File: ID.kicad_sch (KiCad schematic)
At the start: 25 parts

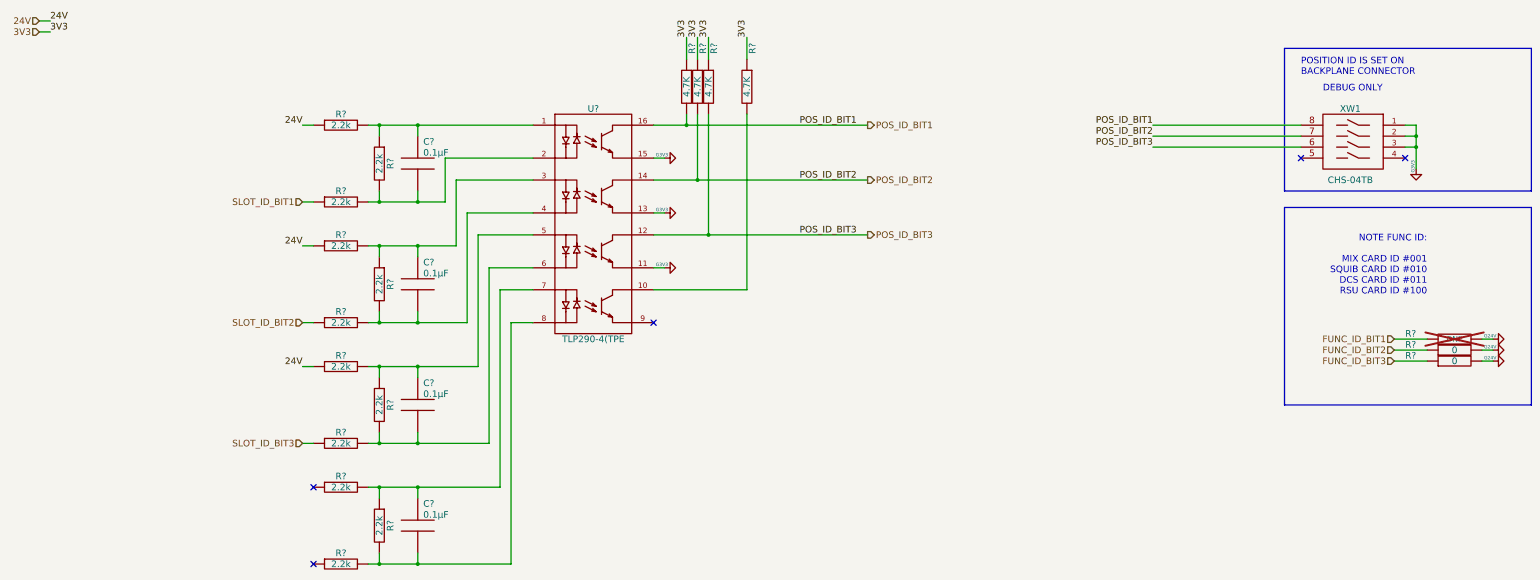
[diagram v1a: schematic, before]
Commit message: kicad 9 - r11-check gerber before sending to manufacturing
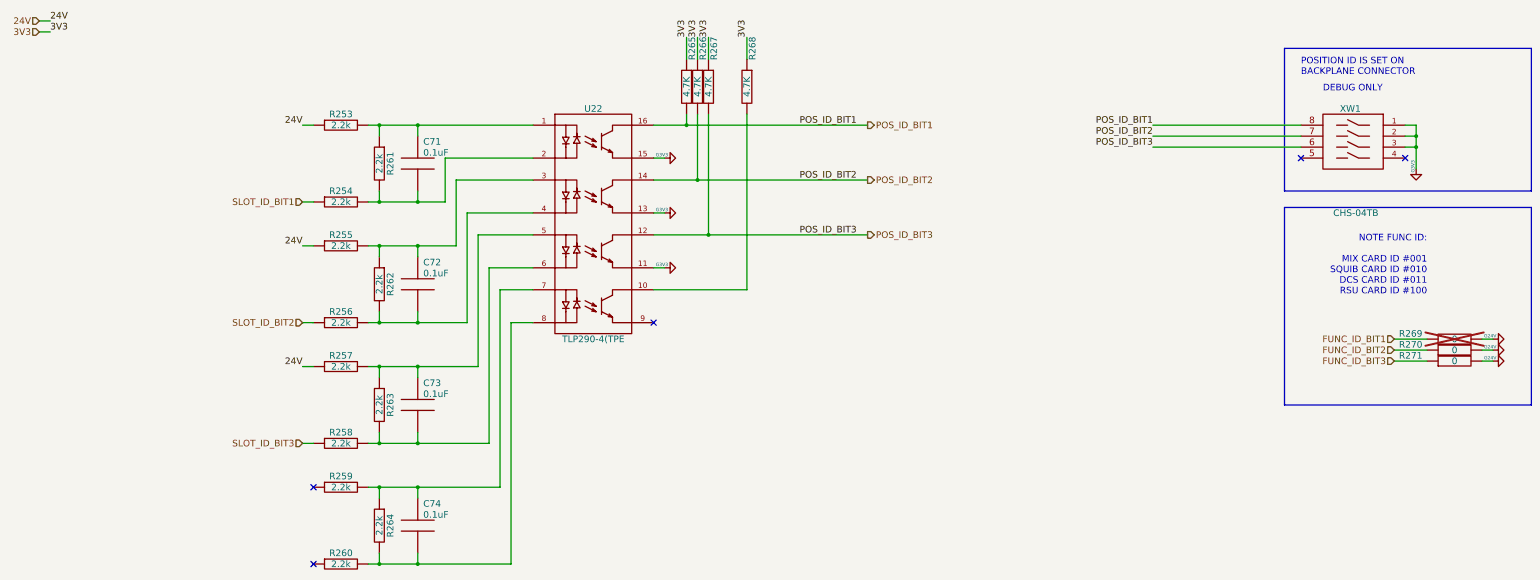
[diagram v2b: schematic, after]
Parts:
- C71, C72, C73, C74: renamed from C?; Nominal 0.1µF -> 0.1uF; SupllierPartNumber 478-3352-1-ND -> (none)
- R261, R262, R263, R264: renamed from R?; SupllierPartNumber 311-2.2KERCT-ND -> (none)
- R265, R266, R267, R268: renamed from R?; SupllierPartNumber 311-4.7KARCT-ND -> (none); Tolerance 5% -> (none)
- R269: renamed from R?; fit_field DNP -> (none)
- U22: renamed from U?; footprint _SOIC_SOP:SOIC127P600X126-16 -> _SOIC_SOP:SOIC127P700X220-16
- XW1: SupllierPartNumber 563-1008-1-ND -> (none)
- gave numbers to parts that had none: 10
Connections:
- net GNDD renamed GND_3V3
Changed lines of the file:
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@@
-(kicad_sch (version 20230819) (generator eeschema)
-  (paper "A3")
-  (title_block
-    (title "EOL ECU MIX CARD")
-    (date "2023-09-26")
-    (rev "0C")
-    (company "ARXTRON TECHNOLOGIES")
-    (comment 1 "A0180-V0")
-    (comment 2 "PRJ22180")
-    (comment 3 "EOL ECU RCM8 RCM9")
-    (comment 4 "ANTON TOKARSKYI")
-  )
+(kicad_sch
+	(version 20250114)
+	(generator "eeschema")
+	(generator_version "9.0")
+	(paper "A3")
+	(title_block
+		(title "EOL ECU MIX CARD")
+		(date "2023-09-26")
+		(rev "0C")
+		(company "ARXTRON TECHNOLOGIES")
+		(comment 1 "A0180-V0")
+		(comment 2 "PRJ22180")
+		(comment 3 "EOL ECU RCM8 RCM9")
+		(comment 4 "ANTON TOKARSKYI")
+	)

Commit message: r11a - clean up mostly with reports naming, values, footprints and parts
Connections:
- net GND_3V3: now also XW1.A1, XW1.A2, XW1.A3; no longer XW1.1, XW1.2, XW1.3
- net POS_ID_BIT1: now also XW1.B1; no longer XW1.8
- net POS_ID_BIT2: now also XW1.B2; no longer XW1.7
- net POS_ID_BIT3: now also XW1.B3; no longer XW1.6
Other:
- company: ARXTRON TECHNOLOGIES -> ${COMPANY}
- title: EOL ECU MIX CARD -> ${PART_NUM} ${PCB_NAME} ${ASSY_VARIANT} ${ASSY_NAME}
- moved on the sheet: XW1
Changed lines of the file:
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@@
 	(paper "A3")
 	(title_block
-		(title "EOL ECU MIX CARD")
-		(date "2023-09-26")
-		(rev "0C")
-		(company "ARXTRON TECHNOLOGIES")
-		(comment 1 "A0180-V0")
-		(comment 2 "PRJ22180")
-		(comment 3 "EOL ECU RCM8 RCM9")
-		(comment 4 "ANTON TOKARSKYI")
+		(title "${PART_NUM} ${PCB_NAME} ${ASSY_VARIANT} ${ASSY_NAME}")
+		(date "2025-03-12")
+		(rev "${REVISION}${REVISION_SCH}")
+		(company "${COMPANY}")
+		(comment 1 "${PART_NUM}")
+		(comment 2 "${PRJ_NUM}")
+		(comment 3 "${PRJ_NAME}")
+		(comment 4 "${DESIGNED}")
+		(comment 5 "${PART_NUM_ICT}")
 	)
